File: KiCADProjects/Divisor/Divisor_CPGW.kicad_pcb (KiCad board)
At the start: 2 copper layers, 94.2 x 94.6 mm, 34 parts, among them J1 SMA_Female, J10 SMA_Female, J11 SMA_Female, J12 SMA_Female, J13 SMA_Female, J14 SMA_Female, J15 SMA_Female, J16 SMA_Female, J17 SMA_Female, J2 SMA_Female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

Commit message: Minor changes
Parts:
- moved J5 27.3 mm to (121.5, 145.1)
- moved J6 27.3 mm to (137.8, 143.5)
- moved R9 27.3 mm to (145.3, 104.5)
- moved J13 27.3 mm to (137.7, 58.0)
- moved J14 27.3 mm to (121.5, 56.5)
- moved R12 27.3 mm to (137.6, 84.9)
- moved R13 27.3 mm to (131.1, 81.6)
- moved R4 27.3 mm to (116.7, 118.7)
- moved J10 27.3 mm to (169.3, 92.6)
- moved J11 27.3 mm to (163.4, 77.4)
- moved J12 27.3 mm to (152.4, 65.3)
- moved J16 27.3 mm to (92.7, 70.8)
- moved J2 27.3 mm to (84.1, 116.8)
- moved J3 27.3 mm to (92.7, 130.7)
- moved J4 27.3 mm to (105.8, 140.6)
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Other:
- board text added: "DIVISOR DE POTENCIA 1 X 16 TELECO IB 2020 REV. C-1.0"
- board text removed: "DIVISOR DE POTENCIA 1 X 16 TELECO IB 2020 REV. M-1.0"

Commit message: Revisión 1.1 de PCBs
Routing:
- net Net-(R1-Pad1): vias 0 -> 1
- net GND: vias 17 -> 34
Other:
- outline, holes or cut-outs redrawn
- net class GND added: clearance 0.5, trace_width 2.4, via_dia 0.9, via_drill 0.7

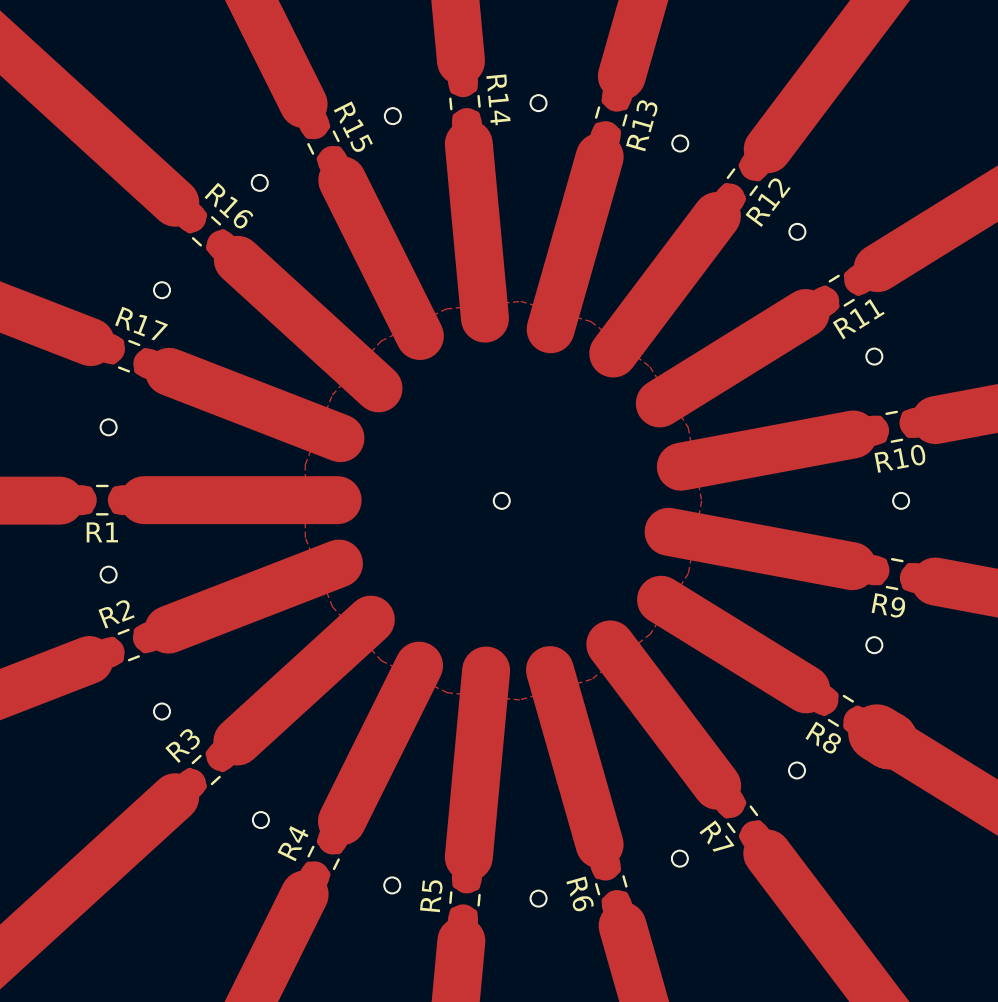
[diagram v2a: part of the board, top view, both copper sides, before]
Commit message: Modificaciones varias al divisor
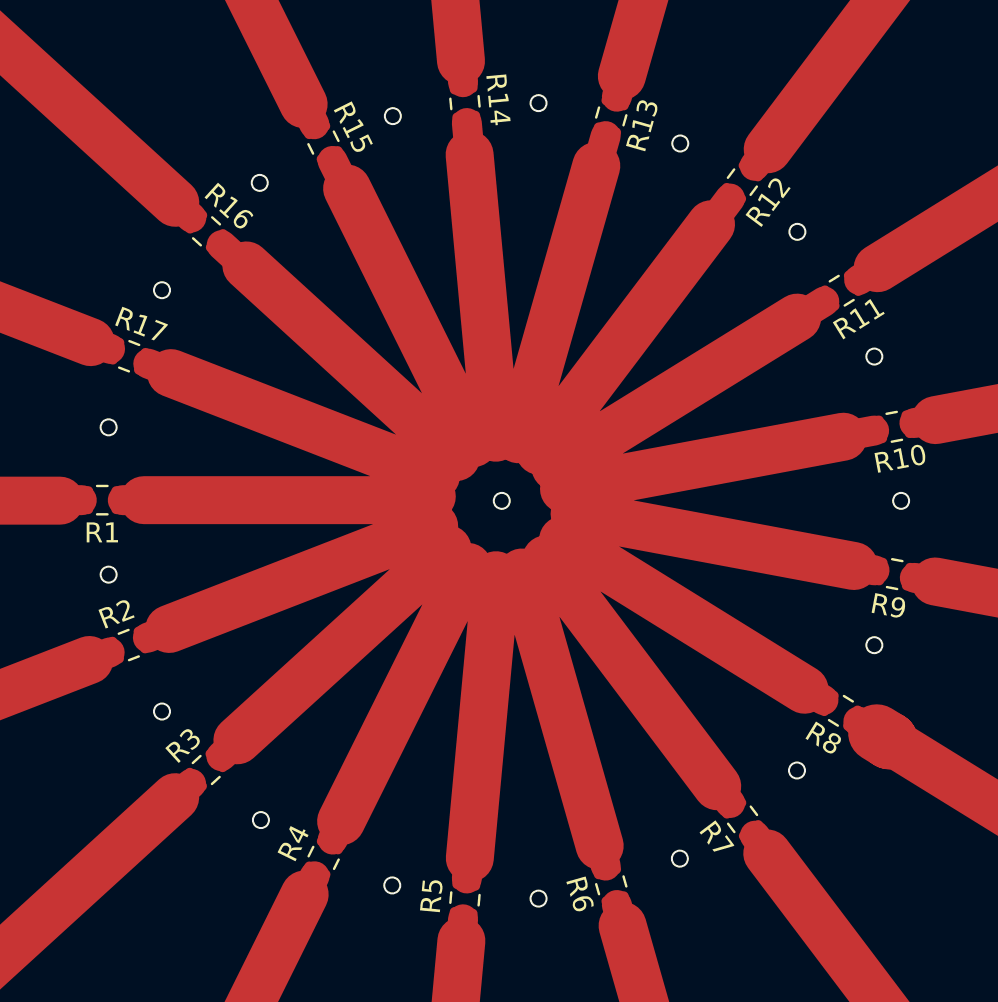
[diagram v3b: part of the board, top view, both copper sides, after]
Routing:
- net Net-(R1-Pad1): track 171.3 -> 260.3 mm
